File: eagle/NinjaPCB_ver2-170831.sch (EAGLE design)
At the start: 86 parts, among them IC1 MCP3551SNNC, IC2 VNH5019/VNH3SP30NC, J2 WELL_TEMP, J3 HEATER, J4 HEATER_TEMP, J5 HEATER_TEMP, Q2 IRF520NPBF, Q3 IRF520NPBF, U1 CJT1117-3.3-SOT223, U2 ESP-12F

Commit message: completed ver2-170831
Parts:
- removed C1: CAP_TH_10UF_50V, Seeed-OPL-2017-01-Capacitor-akita:CAP_TH_10UF_50V
- removed C4, C5, C6: CAP_SMDAL_1000UF_25V, Seeed-OPL-2017-01-Capacitor-akita:CAP_SMDAL_1000UF_25V
- removed I2C, MCU, SPI: (no value), pinhead:PINHD-1X4OCT
- removed R7: 30K, Seeed-Resistor:SMD-RES-30K-1%-1/10W(0603)
- removed R8: 15K 1/10W, Seeed-Resistor:SMD-RES-15K-1%-1/10W(0603)
- removed SJ18, SJ31, SJ32, SJ33, SJ34, SJ35, SJ36: (no value), jumper:SJ
- removed U$2: ATX24, PCR-Connector:ATX24
- removed U$3: ANALOGSW_AD_SOT23-6, PCR-IC:ANALOGSW_AD_SOT23-6
- removed U$4: NAU7802, PCR-IC:NAU7802
- removed U$5: ANALOGSW_TI-SC70-5/6, PCR-IC:ANALOGSW_TI-SC70-5/6
- added C8: CAP_E5-13-L3030RINV, PCR-RCL:CAP_E5-13-L3030RINV
- added IC3: ANALOGSW_AD_SOT23-6NC, PCR-IC:ANALOGSW_AD_SOT23-6NC
- added IC4: ANALOGSW_TI-SC70-5/6NC, PCR-IC:ANALOGSW_TI-SC70-5/6NC
- added IC6: NAU7802NC, PCR-IC:NAU7802NC
- added MODE: (no value), Seeed-Switch:DIP-SWITCH-TACTILE-SPST-NO/TS-1109(4P-D6.0MM)'TS-1109'
- added R12: 10K 1/10W, Seeed-Resistor:SMD-RES-10K-5%-1/10W(0603)
- added RH: 15K 1/10W, PCR-RCL:R0603NC
- added RL: 30K, PCR-RCL:R0603NC
- added SJ37, SJ38, SJ39, SJ40: (no value), jumper:SJ2W
- added WELLEXT1, WELLEXT2, WELL_TEMP: (no value), pinhead:PINHD-1X2
- IC2: value VNH5019/VNH3SP30NC -> VNH5019/VNH3SP30-BNC; device st-microelectronics:VNH5019/VNH3SP30NC -> st-microelectronics:VNH5019/VNH3SP30-BNC
- J2: value WELL_TEMP -> ATX24; device Seeed-Connector:SCREW-TERMINAL-GREEN(2P-3.5) -> PCR-Connector:ATX24
- J5: value HEATER_TEMP -> PELTIER
- R11, R4: device Seeed-Resistor:SMD-RES-1.5K-1%-1/10W(0603) -> PCR-RCL:R0603NC
- SJ17: device jumper:SJ -> jumper:SJ2W
- renumbered IC1 to IC5, U$1 to ESP1, U2 to ESP2
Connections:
- removed net GND1: IC2.GNDA, IC2.GNDA@1, IC2.GNDA@2, IC2.GNDB, IC2.GNDB@1, IC2.GNDB@2
- removed net N$25: IC2.OUTA, IC2.OUTA@1, IC2.OUTA@2, IC2.OUTA@3, IC2.OUTA@4, J5.1
- removed net N$29: SJ36.1, U$4.VIN1P
- removed net N$31: IC5.VIN+, SJ35.1
- removed net N$32: IC2.OUTB, IC2.OUTB@1, IC2.OUTB@2, IC2.OUTB@3, IC2.OUTB@4, J5.2
- removed net N$50: ESP2.MISO, SJ31.1
- removed net N$51: ESP2.MOSI, SJ32.1
- removed net N$52: ESP2.SCLK, SJ33.1
- removed net N$53: ESP2.CS0, SJ34.1
- removed net N$65: ESP2.IO9, SJ17.2
- removed net N$66: ESP2.IO10, SJ18.2
- removed net VCC: R9.1
- new net I2C_WELL_TEMP: IC6.VIN1P, SJ17.3
- new net N$26: WELLEXT1.1, WELLEXT2.1
- new net N$28: WELLEXT1.2, WELLEXT2.2
- new net OUTA: IC2.OUTA@1, IC2.OUTA@2, IC2.OUTA@3, J5.1
- new net OUTB: IC2.OUTB, IC2.OUTB@1, IC2.OUTB@2, IC2.OUTB@3, J5.2
- new net SPI_WELL_TEMP: IC5.VIN+, SJ17.1
- net 12V: now also C8.+, J2.12V_10, J2.12V_11; no longer C1.P$P, C4.P$P, C5.P$P, C6.P$P, IC2.VCC@4, U$2.12V_10, U$2.12V_11
- net 3V3: now also IC3.D, IC3.VDD, IC4.D, IC4.VDD, IC6.AVDD, IC6.DVDD, IC6.REFP, J4.2, MODE.A0, MODE.A1, R9.1, RL.2; no longer J4.1, R7.2, U$3.D, U$3.VDD, U$4.AVDD, U$4.DVDD, U$4.REFP, U$5.D, U$5.VDD
- net EXTADC_I2C_SCL: now also IC6.SCLK, SJ37.3; no longer I2C.1, U$4.SCLK
- net EXTADC_I2C_SDA: now also IC6.SDIO, SJ39.3; no longer I2C.3, U$4.SDIO
- net EXTADC_RDY: now also IC6.DRDY, SJ40.3; no longer I2C.4, U$4.DRDY
- net GND: now also C8.-, IC2.GNDA, IC2.GNDA@1, IC2.GNDA@2, IC2.GNDB, IC2.GNDB@1, IC2.GNDB@2, IC3.GND, IC4.GND, IC6.AVSS, IC6.DVSS, IC6.REFN, J1.CDN, J2.GND15, J2.GND17, J2.GND18, J2.GND19, J2.GND24, J2.GND3, J2.GND5, J2.GND7, R12.1, WELL_TEMP.2; no longer C1.P$M, C4.P$M, C5.P$M, C6.P$M, J2.2, U$2.GND15, U$2.GND17, U$2.GND18, U$2.GND19, U$2.GND24, U$2.GND3, U$2.GND5, U$2.GND7, U$3.GND, U$4.AVSS, U$4.DVSS, U$4.REFN, U$5.GND
- net HIGH_TEMP: now also IC3.IN, IC4.IN, MODE.B0, MODE.B1, R12.2; no longer U$3.IN, U$5.IN
- net IO12: now also SJ38.2; no longer MCU.2
- net IO14: now also SJ37.2; no longer MCU.1
- net IO2: now also SJ39.2; no longer MCU.3
- net IO5: now also SJ40.2; no longer MCU.4
- net N$1: now also J4.1; no longer J4.2
- net N$27: now also IC3.S, IC4.S, RH.1; no longer R8.1, U$3.S, U$5.S
- net N$61: now also ESP2.MISO; no longer SJ31.2
- net N$62: now also ESP2.MOSI; no longer SJ32.2
- net N$63: now also ESP2.SCLK; no longer SJ33.2
- net N$64: now also ESP2.CS0; no longer SJ34.2
- net N$72: now also ESP2.IO9; no longer SJ17.1
- net N$73: now also ESP2.IO10; no longer SJ18.1
- net N$91: now also IC6.VIN1N; no longer U$4.VIN1N
- net N$92: now also IC6.VBG; no longer U$4.VBG
- net PEL_INA: now also SJ38.3, SJ39.1; no longer I2C.2, SPI.3
- net SPI_CS: now also SJ40.1; no longer SPI.4
- net SPI_SCK: now also SJ37.1; no longer SPI.1
- net SPI_SDO: now also SJ38.1; no longer SPI.2
- net WELL_TEMP: now also RH.2, RL.1, SJ17.2, WELL_TEMP.1; no longer J2.1, R7.1, R8.2, SJ35.2, SJ36.2
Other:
- moved on the sheet: C7, J4

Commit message: completed ver2-170831
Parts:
- removed J1: (no value), Seeed-Connector:JACK-DC-005'DC-005'
- added U$1: 2.1MMJACKTHM, adafruit:2.1MMJACKTHM
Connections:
- net 12V: now also U$1.TIP; no longer J1.+
- net GND: now also U$1.RING, U$1.RING_SW; no longer J1.-, J1.CDN
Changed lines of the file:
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@@
 <setting verticaltext="up"/>
 </settings>
-<grid distance="0.1" unitdist="inch" unit="inch" style="lines" multiple="1" display="no" altdistance="0.01" altunitdist="inch" altunit="inch"/>
+<grid distance="0.05" unitdist="inch" unit="inch" style="lines" multiple="1" display="no" altdistance="0.01" altunitdist="inch" altunit="inch"/>
 <layers>
 <layer number="1" name="Top" color="4" fill="1" visible="yes" active="no"/>
@@
 <part name="P+1" library="supply1" deviceset="VCC" device="" value="3V3"/>
 <part name="GND3" library="supply1" deviceset="GND" device=""/>
-<part name="J1" library="Seeed-Connector" deviceset="JACK-DC-005" device="'DC-005'"/>
 <part name="P+2" library="supply1" deviceset="VCC" device="" value="12V"/>
 <part name="FRAME1" library="frames" deviceset="A3L-LOC" device=""/>
@@
 <part name="SJ17" library="jumper" deviceset="SJ2W" device=""/>
 <part name="IC2" library="st-microelectronics" deviceset="VNH5019/VNH3SP30-B" device="NC" value="VNH5019/VNH3SP30-BNC"/>
+<part name="U$1" library="adafruit" deviceset="2.1MMJACK" device="THM"/>
 </parts>
 <sheets>
@@
 <instance part="P+1" gate="VCC" x="248.92" y="180.34"/>
 <instance part="GND3" gate="1" x="248.92" y="148.59"/>
-<instance part="J1" gate="JACK" x="96.52" y="53.34"/>
 <instance part="P+2" gate="VCC" x="106.68" y="60.96"/>
 <instance part="FRAME1" gate="G$1" x="0" y="0"/>
@@
 <instance part="SJ17" gate="G$1" x="261.62" y="139.7" rot="MR0"/>
 <instance part="IC2" gate="G$1" x="325.12" y="214.63"/>
+<instance part="U$1" gate="G$1" x="97.79" y="53.34"/>
 </instances>
 <busses>
@@
 <wire x1="102.87" y1="50.8" x2="106.68" y2="50.8" width="0.1524" layer="91"/>
 <wire x1="106.68" y1="50.8" x2="106.68" y2="45.72" width="0.1524" layer="91"/>
-<pinref part="J1" gate="JACK" pin="-"/>
-<pinref part="J1" gate="JACK" pin="CDN"/>
 <wire x1="102.87" y1="53.34" x2="106.68" y2="53.34" width="0.1524" layer="91"/>
 <wire x1="106.68" y1="53.34" x2="106.68" y2="50.8" width="0.1524" layer="91"/>
 <junction x="106.68" y="50.8"/>
+<pinref part="U$1" gate="G$1" pin="RING"/>
+<pinref part="U$1" gate="G$1" pin="RING_SW"/>
 </segment>
 <segment>
@@
 <net name="12V" class="0">
 <segment>
-<pinref part="J1" gate="JACK" pin="+"/>
 <pinref part="P+2" gate="VCC" pin="VCC"/>
 <wire x1="102.87" y1="55.88" x2="106.68" y2="55.88" width="0.1524" layer="91"/>
 <wire x1="106.68" y1="55.88" x2="106.68" y2="58.42" width="0.1524" layer="91"/>
-</segment>
-<segment>
+<pinref part="U$1" gate="G$1" pin="TIP"/>
+</segment>
+<segment>

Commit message: completed ver2-170831
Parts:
- removed CS0, IO10, IO9, MISO, MOSI, SCKL: (no value), pinhead:PINHD-1X1
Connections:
- removed net N$61: ESP2.MISO, MISO.1
- removed net N$62: ESP2.MOSI, MOSI.1
- removed net N$63: ESP2.SCLK, SCKL.1
- removed net N$64: CS0.1, ESP2.CS0
- removed net N$72: ESP2.IO9, IO9.1
- removed net N$73: ESP2.IO10, IO10.1
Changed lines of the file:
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@@
 <part name="GND15" library="supply1" deviceset="GND" device=""/>
 <part name="C3" library="Seeed-Capacitor" deviceset="CERAMIC-100NF-50V-10%-X7R(0603)" device="" value="100nf"/>
-<part name="IO9" library="pinhead" deviceset="PINHD-1X1" device=""/>
-<part name="IO10" library="pinhead" deviceset="PINHD-1X1" device=""/>
-<part name="MISO" library="pinhead" deviceset="PINHD-1X1" device=""/>
-<part name="MOSI" library="pinhead" deviceset="PINHD-1X1" device=""/>
-<part name="SCKL" library="pinhead" deviceset="PINHD-1X1" device=""/>
-<part name="CS0" library="pinhead" deviceset="PINHD-1X1" device=""/>
 <part name="R10" library="Seeed-Resistor" deviceset="SMD-RES-3K-1%-1/10W(0603)" device="" value="3K"/>
 <part name="R14" library="Seeed-Resistor" deviceset="SMD-RES-2K-1%-1/10W(0603)" device="" value="2K"/>
@@
 <instance part="GND15" gate="1" x="190.5" y="85.09"/>
 <instance part="C3" gate="G$1" x="190.5" y="104.14" rot="R90"/>
-<instance part="IO9" gate="G$1" x="16.51" y="158.75" rot="MR0"/>
-<instance part="IO10" gate="G$1" x="16.51" y="149.86" rot="MR0"/>
-<instance part="MISO" gate="G$1" x="120.65" y="146.05"/>
-<instance part="MOSI" gate="G$1" x="120.65" y="137.16"/>
-<instance part="SCKL" gate="G$1" x="120.65" y="128.27"/>
-<instance part="CS0" gate="G$1" x="120.65" y="119.38"/>
 <instance part="R10" gate="G$1" x="314.96" y="154.94"/>
 <instance part="R14" gate="G$1" x="314.96" y="148.59"/>
@@
 </segment>
 </net>
-<net name="N$61" class="0">
-<segment>
-<wire x1="111.76" y1="144.78" x2="111.76" y2="146.05" width="0.1524" layer="91"/>
-<wire x1="111.76" y1="146.05" x2="118.11" y2="146.05" width="0.1524" layer="91"/>
-<pinref part="MISO" gate="G$1" pin="1"/>
-<pinref part="ESP2" gate="G$1" pin="MISO"/>
-<wire x1="111.76" y1="144.78" x2="91.44" y2="144.78" width="0.1524" layer="91"/>
-</segment>
-</net>
-<net name="N$62" class="0">
-<segment>
-<wire x1="111.76" y1="142.24" x2="111.76" y2="137.16" width="0.1524" layer="91"/>
-<wire x1="111.76" y1="137.16" x2="118.11" y2="137.16" width="0.1524" layer="91"/>
-<pinref part="MOSI" gate="G$1" pin="1"/>
-<pinref part="ESP2" gate="G$1" pin="MOSI"/>
-<wire x1="111.76" y1="142.24" x2="91.44" y2="142.24" width="0.1524" layer="91"/>
-</segment>
-</net>
-<net name="N$63" class="0">
-<segment>
-<wire x1="109.22" y1="139.7" x2="109.22" y2="128.27" width="0.1524" layer="91"/>
-<wire x1="109.22" y1="128.27" x2="118.11" y2="128.27" width="0.1524" layer="91"/>
-<pinref part="SCKL" gate="G$1" pin="1"/>
-<pinref part="ESP2" gate="G$1" pin="SCLK"/>
-<wire x1="109.22" y1="139.7" x2="91.44" y2="139.7" width="0.1524" layer="91"/>
-</segment>
-</net>
-<net name="N$64" class="0">
-<segment>
-<wire x1="106.68" y1="137.16" x2="106.68" y2="119.38" width="0.1524" layer="91"/>
-<wire x1="106.68" y1="119.38" x2="118.11" y2="119.38" width="0.1524" layer="91"/>
-<pinref part="CS0" gate="G$1" pin="1"/>
-<pinref part="ESP2" gate="G$1" pin="CS0"/>
-<wire x1="106.68" y1="137.16" x2="91.44" y2="137.16" width="0.1524" layer="91"/>
-</segment>
-</net>
 <net name="N$67" class="0">
 <segment>
@@
 </segment>
 </net>
-<net name="N$72" class="0">
-<segment>
-<wire x1="55.88" y1="154.94" x2="24.13" y2="154.94" width="0.1524" layer="91"/>
-<wire x1="24.13" y1="154.94" x2="24.13" y2="158.75" width="0.1524" layer="91"/>
-<wire x1="24.13" y1="158.75" x2="19.05" y2="158.75" width="0.1524" layer="91"/>
-<pinref part="IO9" gate="G$1" pin="1"/>
-<pinref part="ESP2" gate="G$1" pin="IO9"/>
-</segment>
-</net>
-<net name="N$73" class="0">
-<segment>
-<wire x1="55.88" y1="152.4" x2="24.13" y2="152.4" width="0.1524" layer="91"/>
-<wire x1="24.13" y1="152.4" x2="24.13" y2="149.86" width="0.1524" layer="91"/>
-<wire x1="24.13" y1="149.86" x2="19.05" y2="149.86" width="0.1524" layer="91"/>
-<pinref part="IO10" gate="G$1" pin="1"/>
-<pinref part="ESP2" gate="G$1" pin="IO10"/>
-</segment>
-</net>

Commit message: completed ver2-170831
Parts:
- added RH2: 30K HP, PCR-RCL:R0603NC
- RD1, RD2: value 1.5K or 1.8K -> 30K HP
- RH1: value 15K 1/10W -> 30K HP
- RL: value 30K -> 30K HP
- renumbered R11 to RD2, R4 to RD1, RH to RH1
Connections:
- net N$27: now also RH2.1
- net WELL_TEMP: now also RH2.2

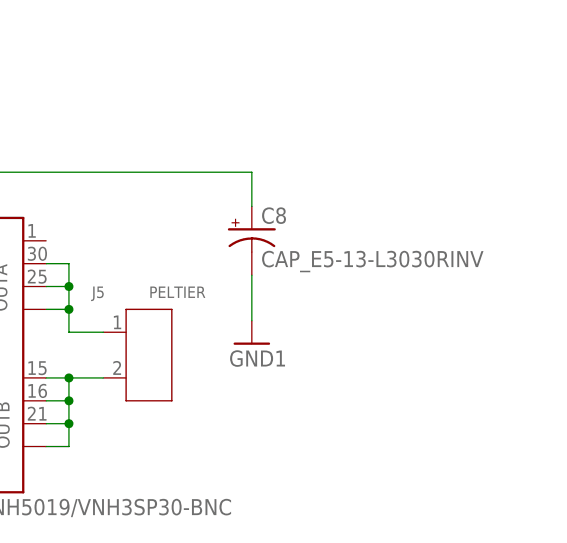
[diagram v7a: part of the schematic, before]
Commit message: remove ver2 temporary. it will be back after evaluation.
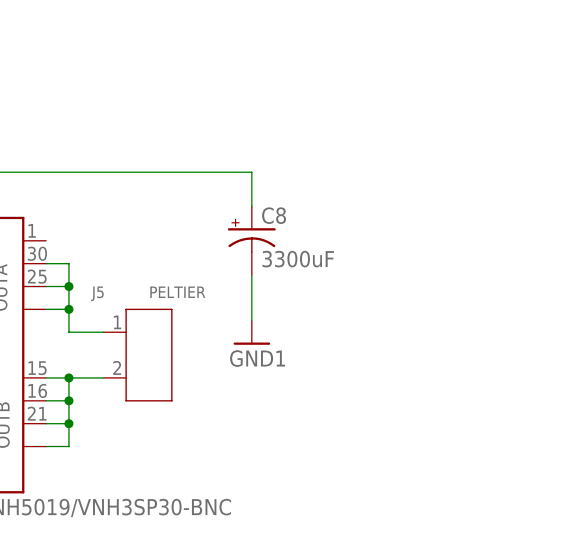
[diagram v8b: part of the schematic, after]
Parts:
- C8: value CAP_E5-13-L3030RINV -> 3300uF
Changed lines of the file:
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@@
 <part name="SJ39" library="jumper" deviceset="SJ2W" device=""/>
 <part name="SJ40" library="jumper" deviceset="SJ2W" device=""/>
-<part name="C8" library="PCR-RCL" deviceset="CAP_E5-13-L30" device="30RINV" value="CAP_E5-13-L3030RINV"/>
+<part name="C8" library="PCR-RCL" deviceset="CAP_E5-13-L30" device="30RINV" value="3300uF"/>
 <part name="GND21" library="openpcr" deviceset="GND1" device=""/>
 <part name="SJ17" library="jumper" deviceset="SJ2W" device=""/>
